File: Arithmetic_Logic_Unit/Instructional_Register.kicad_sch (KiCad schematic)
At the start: 19 parts, among them IC3 SN54173J, IC4 SN54173J, U2 74LS245

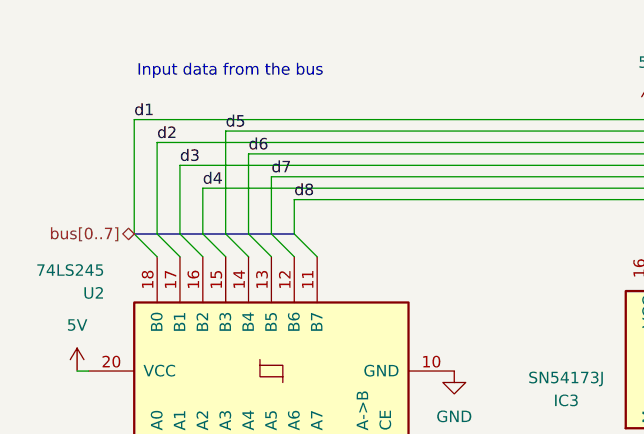
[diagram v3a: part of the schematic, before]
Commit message: completed alu schematic with errors
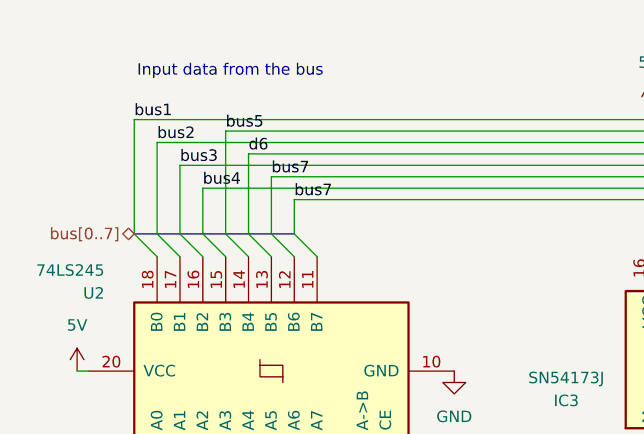
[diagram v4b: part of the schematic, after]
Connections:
- net d8 is gone; now on net bus7: IC4.11 (4D)
- net d2 renamed bus2
- net d3 renamed bus3
- net d4 renamed bus4
- net d5 renamed bus5
- net d7 renamed bus7
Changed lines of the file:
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@@
 		)
 	)
-	(label "d2"
+	(label "bus2"
 		(at 44.45 40.64 0)
 		(fields_autoplaced yes)
@@
 		)
 	)
-	(label "d4"
+	(label "bus4"
 		(at 49.53 45.72 0)
 		(fields_autoplaced yes)
@@
 		)
 	)
-	(label "d1"
+	(label "bus1"
 		(at 41.91 38.1 0)
 		(fields_autoplaced yes)
@@
 		)
 	)
-	(label "d8"
+	(label "bus7"
 		(at 59.69 46.99 0)
 		(fields_autoplaced yes)
@@
 		)
 	)
-	(label "d3"
+	(label "bus3"
 		(at 46.99 43.18 0)
 		(fields_autoplaced yes)
@@
 		)
 	)
-	(label "d7"
+	(label "bus7"
 		(at 57.15 44.45 0)
 		(fields_autoplaced yes)
@@
 		)
 	)
-	(label "d5"
+	(label "bus5"
 		(at 52.07 39.37 0)
 		(fields_autoplaced yes)
